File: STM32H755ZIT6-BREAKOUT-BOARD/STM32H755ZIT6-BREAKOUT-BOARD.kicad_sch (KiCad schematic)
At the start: 30 parts, among them U1 STM32H755ZITx

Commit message: more schematic
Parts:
- added C2, C3: 26p, symbol Device:C
- added C30, C4: 15p, symbol Device:C
- added R2: 255, symbol Device:R
- added R3: 32.38k, symbol Device:R
- added Y1: 32.768 kHz, symbol Device:Crystal
- added Y3: 24 MHz, symbol Device:Crystal_GND23
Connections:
- net GND: now also C2.2, C3.1, C30.2, C4.2, Y3.2, Y3.3
- net HSE_IN: now reaches U1.25 (PH0)
- net HSE_IN: now also C2.1, Y3.4
- net HSE_OUT: now reaches U1.26 (PH1)
- net HSE_OUT: now also R2.2
- net NRST: now reaches U1.27 (NRST)
- net LSE_IN: now reaches U1.74 (PB14)
- net LSE_IN: now also C4.1, Y1.2
- net LSE_OUT: now reaches U1.75 (PB15)
- net LSE_OUT: now also R3.2
- new net: C3.2, R2.1, Y3.1
- new net: C30.1, R3.1, Y1.1
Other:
- note added: "High speed external oscillator STM application note: AN2867 - 3.1"
- note added: "Low speed external oscillator STM application note: AN2867 - 3.1"
- note added: "crystal: 12.5pF"
- note added: "crystal: 18pF"

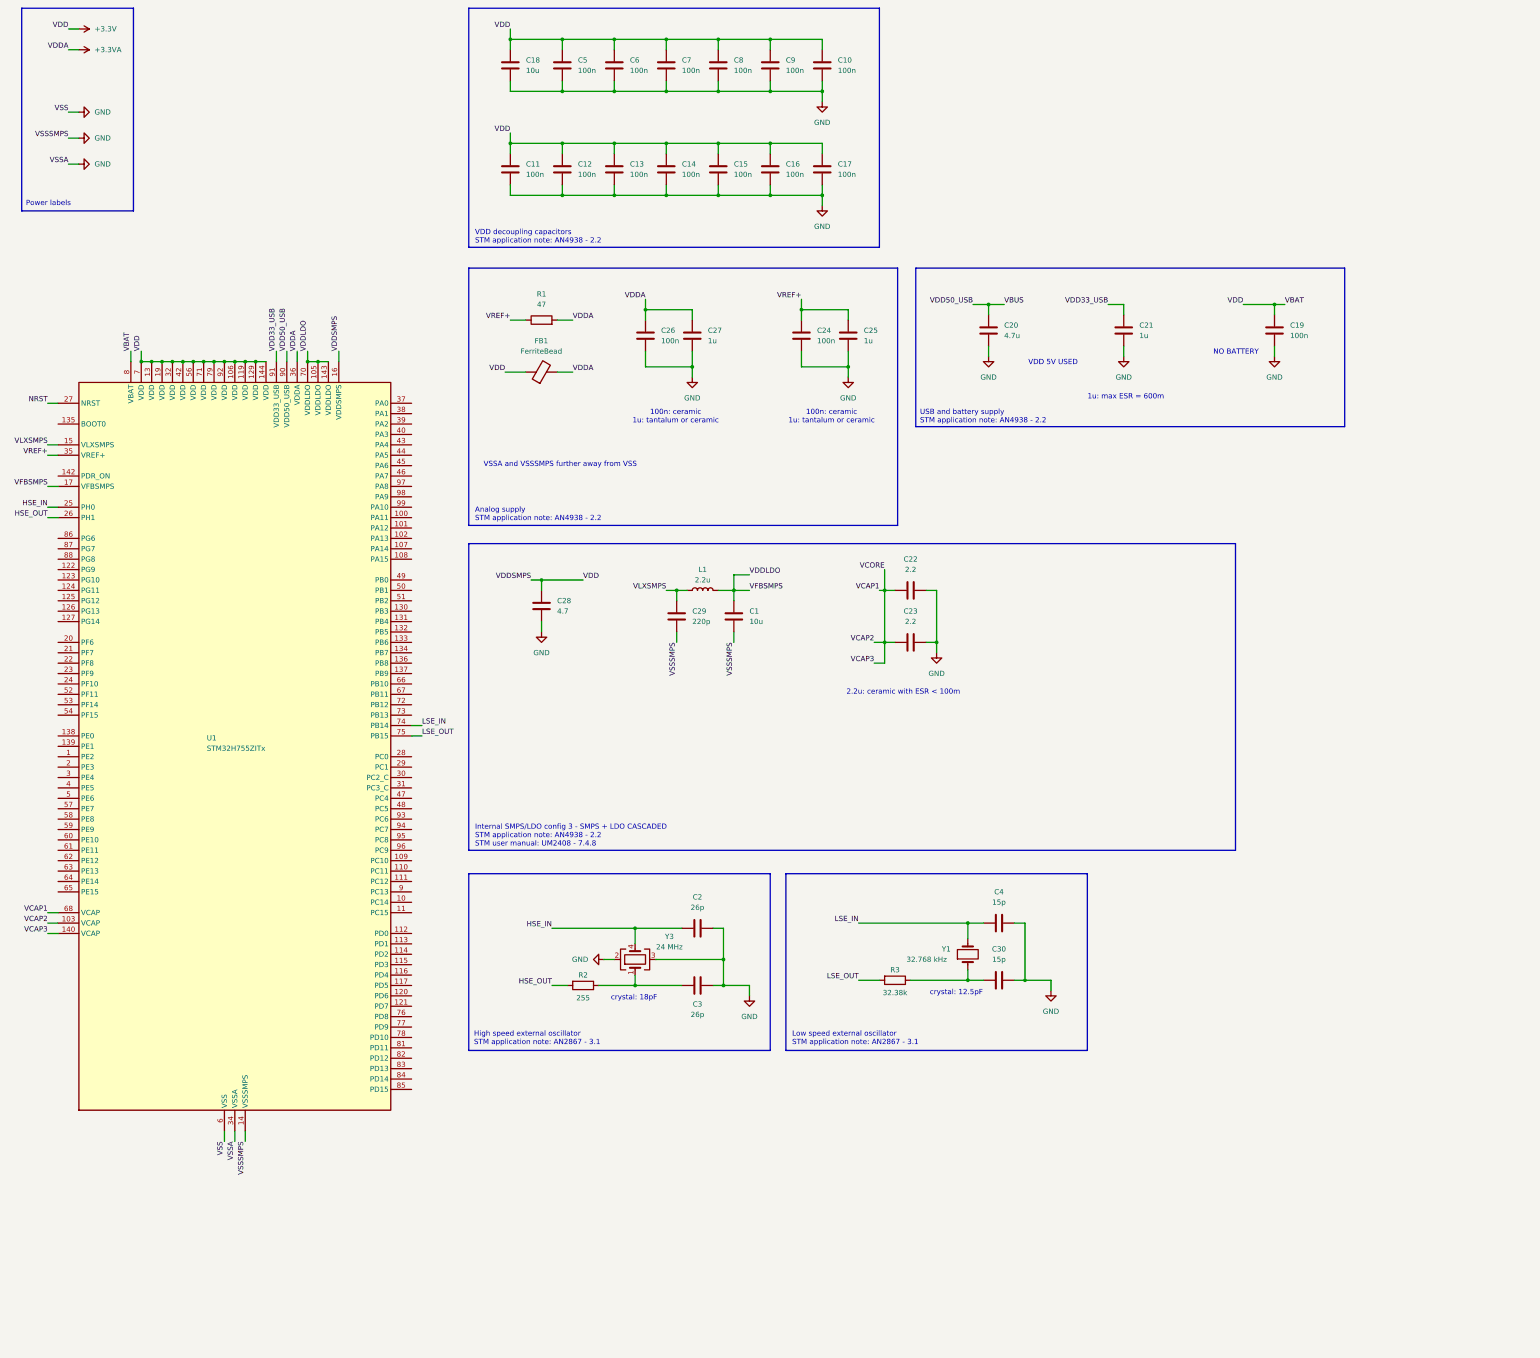
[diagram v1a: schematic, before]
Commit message: schematic pin labels
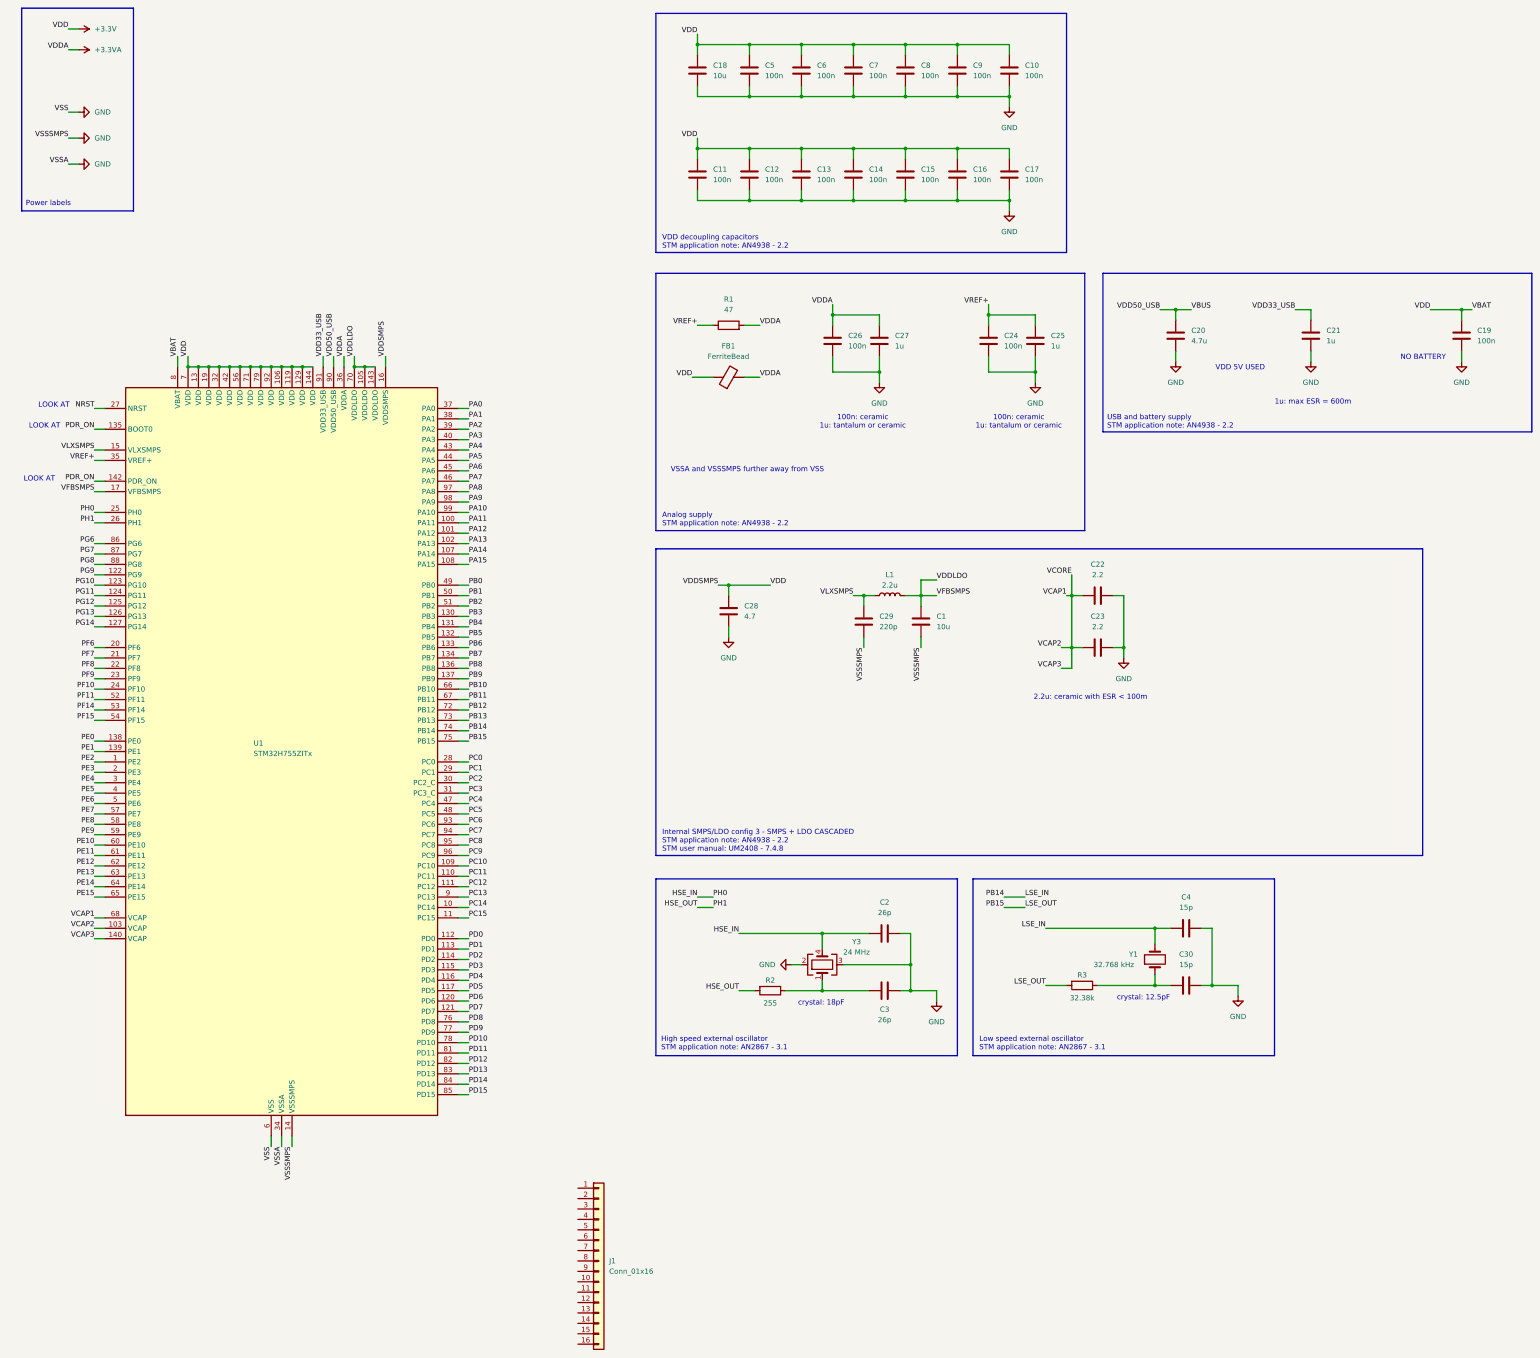
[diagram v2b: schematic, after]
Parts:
- added J1: Conn_01x16, Connector_PinHeader_1.00mm:PinHeader_1x16_P1.00mm_Vertical, symbol Connector_Generic:Conn_01x16
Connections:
- net PE2: now reaches U1.1 (PE2)
- net PC14: now reaches U1.10 (PC14)
- net PA11: now reaches U1.100 (PA11)
- net PA12: now reaches U1.101 (PA12)
- net PA13: now reaches U1.102 (PA13)
- net PA14: now reaches U1.107 (PA14)
- net PA15: now reaches U1.108 (PA15)
- net PC10: now reaches U1.109 (PC10)
- net PC15: now reaches U1.11 (PC15)
- net PC11: now reaches U1.110 (PC11)
- net PC12: now reaches U1.111 (PC12)
- net PD0: now reaches U1.112 (PD0)
- net PD1: now reaches U1.113 (PD1)
- net PD2: now reaches U1.114 (PD2)
- net PD3: now reaches U1.115 (PD3)
- net PD4: now reaches U1.116 (PD4)
- net PD5: now reaches U1.117 (PD5)
- net PD6: now reaches U1.120 (PD6)
- net PD7: now reaches U1.121 (PD7)
- net PG9: now reaches U1.122 (PG9)
- net PG10: now reaches U1.123 (PG10)
- net PG11: now reaches U1.124 (PG11)
- net PG12: now reaches U1.125 (PG12)
- net PG13: now reaches U1.126 (PG13)
- net PG14: now reaches U1.127 (PG14)
- net PB3: now reaches U1.130 (PB3)
- net PB4: now reaches U1.131 (PB4)
- net PB5: now reaches U1.132 (PB5)
- net PB6: now reaches U1.133 (PB6)
- net PB7: now reaches U1.134 (PB7)
- net PDR_ON: now reaches U1.135 (BOOT0)
- net PDR_ON: now also U1.142 (PDR_ON)
- net PB8: now reaches U1.136 (PB8)
- net PB9: now reaches U1.137 (PB9)
- net PE0: now reaches U1.138 (PE0)
- net PE1: now reaches U1.139 (PE1)
- net PE3: now reaches U1.2 (PE3)
- net PF6: now reaches U1.20 (PF6)
- net PF7: now reaches U1.21 (PF7)
- net PF8: now reaches U1.22 (PF8)
- net PF9: now reaches U1.23 (PF9)
- net PF10: now reaches U1.24 (PF10)
- net PC0: now reaches U1.28 (PC0)
- net PC1: now reaches U1.29 (PC1)
- net PE4: now reaches U1.3 (PE4)
- net PC2: now reaches U1.30 (PC2_C)
- net PC3: now reaches U1.31 (PC3_C)
- net PA0: now reaches U1.37 (PA0)
- net PA1: now reaches U1.38 (PA1)
- net PA2: now reaches U1.39 (PA2)
- net PE5: now reaches U1.4 (PE5)
- net PA3: now reaches U1.40 (PA3)
- net PA4: now reaches U1.43 (PA4)
- net PA5: now reaches U1.44 (PA5)
- net PA6: now reaches U1.45 (PA6)
- net PA7: now reaches U1.46 (PA7)
- net PC4: now reaches U1.47 (PC4)
- net PC5: now reaches U1.48 (PC5)
- net PB0: now reaches U1.49 (PB0)
- net PE6: now reaches U1.5 (PE6)
- net PB1: now reaches U1.50 (PB1)
- net PB2: now reaches U1.51 (PB2)
- net PF11: now reaches U1.52 (PF11)
- net PF14: now reaches U1.53 (PF14)
- net PF15: now reaches U1.54 (PF15)
- net PE7: now reaches U1.57 (PE7)
- net PE8: now reaches U1.58 (PE8)
- net PE9: now reaches U1.59 (PE9)
- net PE10: now reaches U1.60 (PE10)
- net PE11: now reaches U1.61 (PE11)
- net PE12: now reaches U1.62 (PE12)
- net PE13: now reaches U1.63 (PE13)
- net PE14: now reaches U1.64 (PE14)
- net PE15: now reaches U1.65 (PE15)
- net PB10: now reaches U1.66 (PB10)
- net PB11: now reaches U1.67 (PB11)
- net PB12: now reaches U1.72 (PB12)
- net PB13: now reaches U1.73 (PB13)
- net PD8: now reaches U1.76 (PD8)
- net PD9: now reaches U1.77 (PD9)
- net PD10: now reaches U1.78 (PD10)
- net PD11: now reaches U1.81 (PD11)
- net PD12: now reaches U1.82 (PD12)
- net PD13: now reaches U1.83 (PD13)
- net PD14: now reaches U1.84 (PD14)
- net PD15: now reaches U1.85 (PD15)
- net PG6: now reaches U1.86 (PG6)
- net PG7: now reaches U1.87 (PG7)
- net PG8: now reaches U1.88 (PG8)
- net PC13: now reaches U1.9 (PC13)
- net PC6: now reaches U1.93 (PC6)
- net PC7: now reaches U1.94 (PC7)
- net PC8: now reaches U1.95 (PC8)
- net PC9: now reaches U1.96 (PC9)
- net PA8: now reaches U1.97 (PA8)
- net PA9: now reaches U1.98 (PA9)
- net PA10: now reaches U1.99 (PA10)
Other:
- note added: "LOOK AT"
- moved on the sheet: C1, C10, C11, C12, C13, C14, C15, C16, C17, C18, C19, C2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

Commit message: pinheaders
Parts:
- removed J1: Conn_01x16, Connector_PinHeader_1.00mm:PinHeader_1x16_P1.00mm_Vertical, symbol Connector_Generic:Conn_01x16
- added J1, J3, J4: Conn_02x16_Odd_Even, Connector_PinHeader_2.54mm:PinHeader_2x16_P2.54mm_Vertical, symbol Connector_Generic:Conn_02x16_Odd_Even
- added J2: Conn_ST_STDC14, Connector_PinHeader_2.54mm:PinHeader_2x07_P2.54mm_Vertical, symbol Connector:Conn_ST_STDC14
- added R10, R11, R4, R5, R6, R7, R9: 22, symbol Device:R
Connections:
- net PB3 is gone; now on net JTDO/SWO: U1.130 (PB3)
- net +3.3V: now also J2.3 (VCC)
- net GND: now also J2.11 (GNDDetect), J2.5 (GND), J2.7 (GND)
- net NRST: now also R4.2
- net PDR_ON: no longer U1.135 (BOOT0)
- net PA13 renamed JTMS/SWDIO
- net JTMS/SWDIO: now also R6.2
- net PA14 renamed JTDO/SWO
- net JTDO/SWO: now also R7.2
- net PA15 renamed JTDI
- net JTDI: now also R9.2
- new net: J2.6 (JCLK/SWCLK), R5.1
- new net: J2.10 (JTDI/NC), R9.1
- new net: J2.12 (~{RST}), R4.1
- new net: J2.13 (VCP_RX), R10.1
- new net: J2.14 (VCP_TX), R11.1
- new net: J2.4 (JTMS/SWDIO), R6.1
- new net: J2.8 (JTDO/SWO), R7.1
- new net BOOT0: U1.135 (BOOT0)
- new net JTCK/SWCLK: R5.2
- no-connect marks 0 -> 1
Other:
- note added: "3.3V supply"

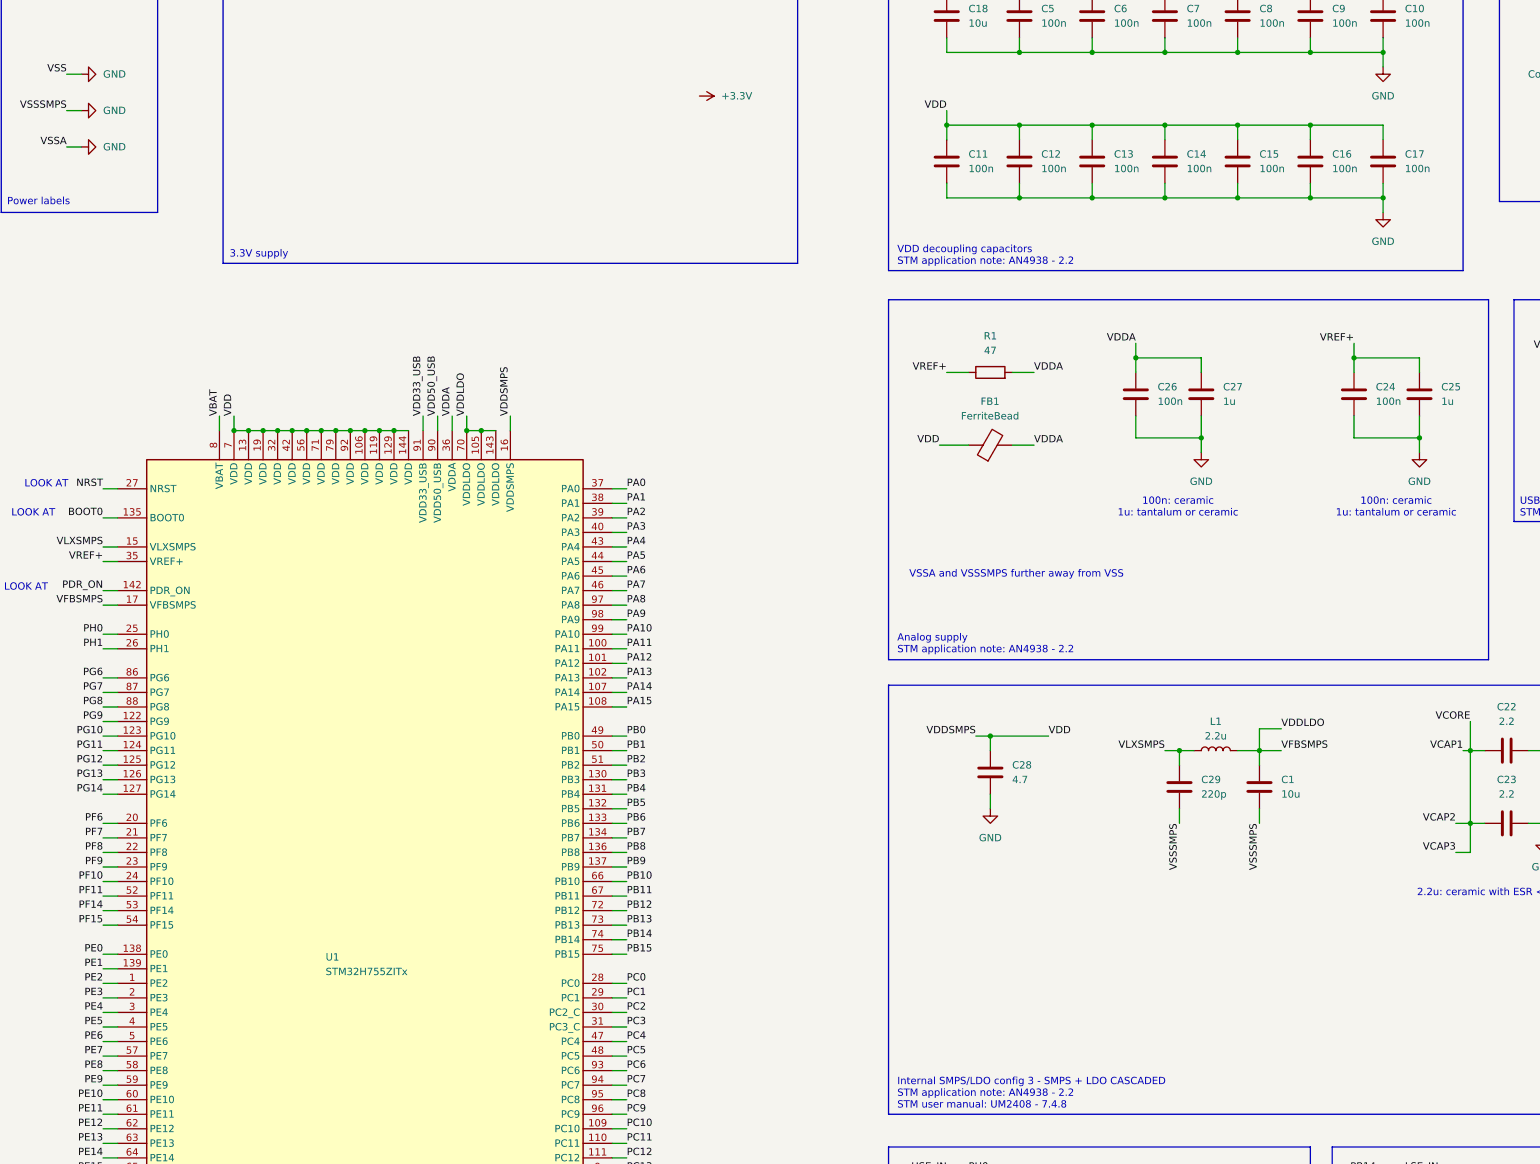
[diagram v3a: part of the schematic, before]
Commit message: edited internal SMPS
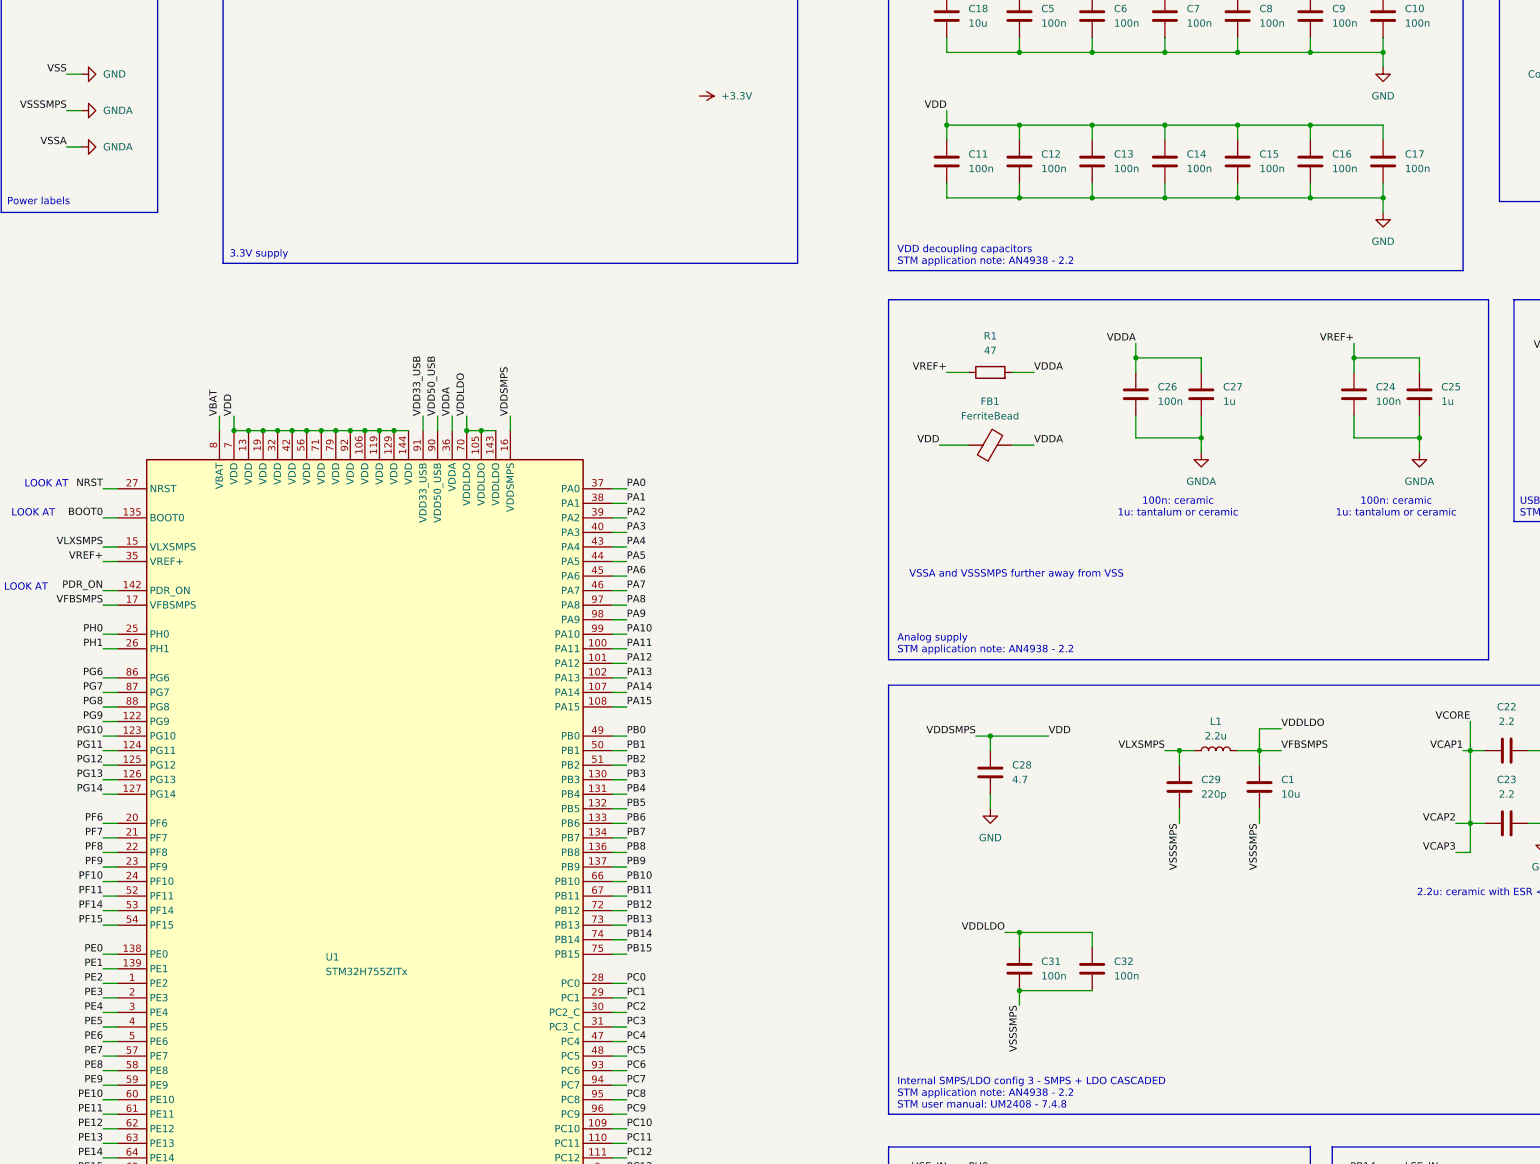
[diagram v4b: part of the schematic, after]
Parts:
- added C31, C32: 100n, symbol Device:C
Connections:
- net GND: no longer C1.2, C24.2, C25.2, C26.2, C27.2, C29.1, U1.14 (VSSSMPS), U1.34 (VSSA)
- net VDDLDO: now also C31.2, C32.2
- new net GNDA: C1.2, C24.2, C25.2, C26.2, C27.2, C29.1, C31.1, C32.1, U1.14 (VSSSMPS), U1.34 (VSSA)
